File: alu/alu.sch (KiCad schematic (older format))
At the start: 38 parts

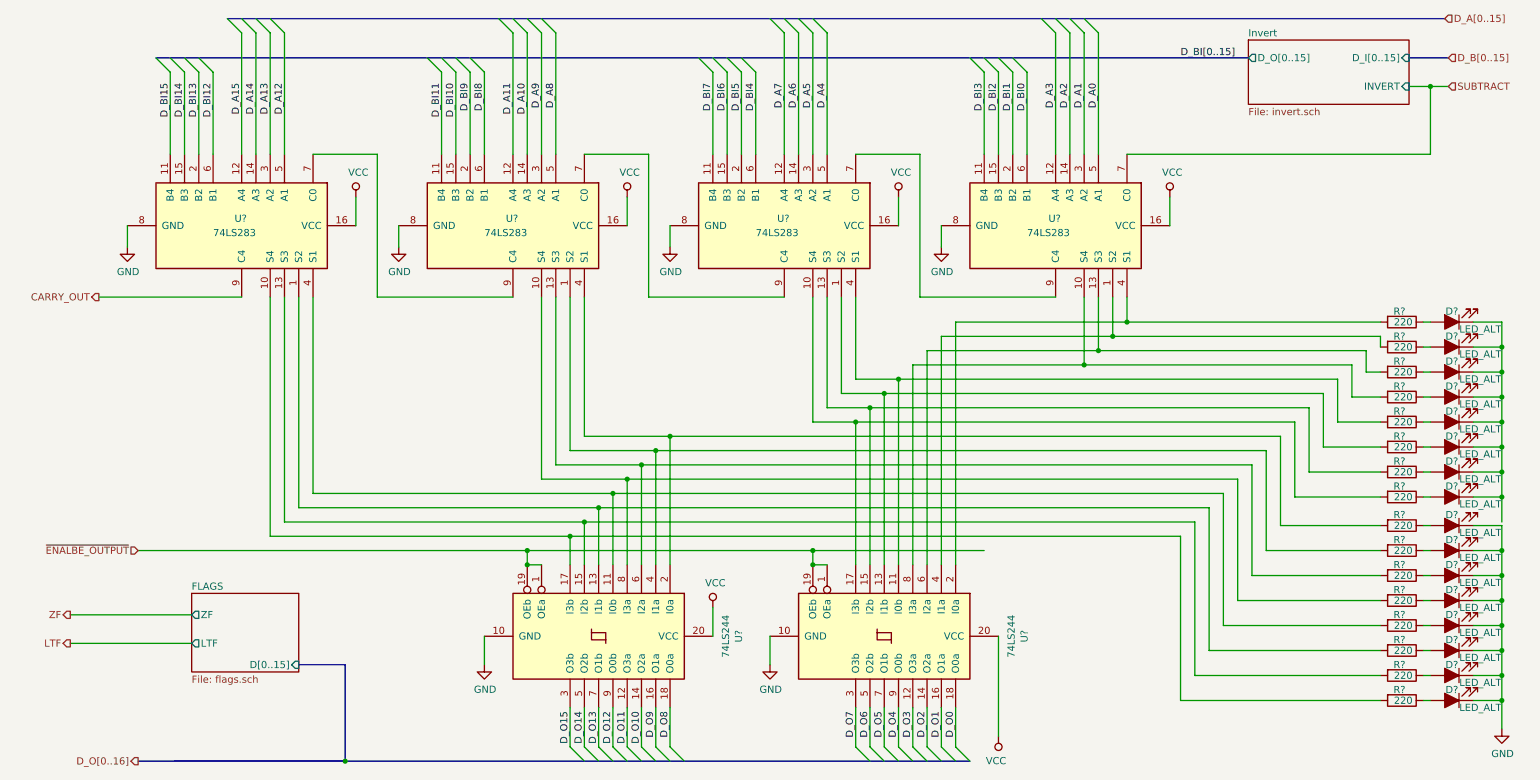
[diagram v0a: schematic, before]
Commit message: alu routed first iteration
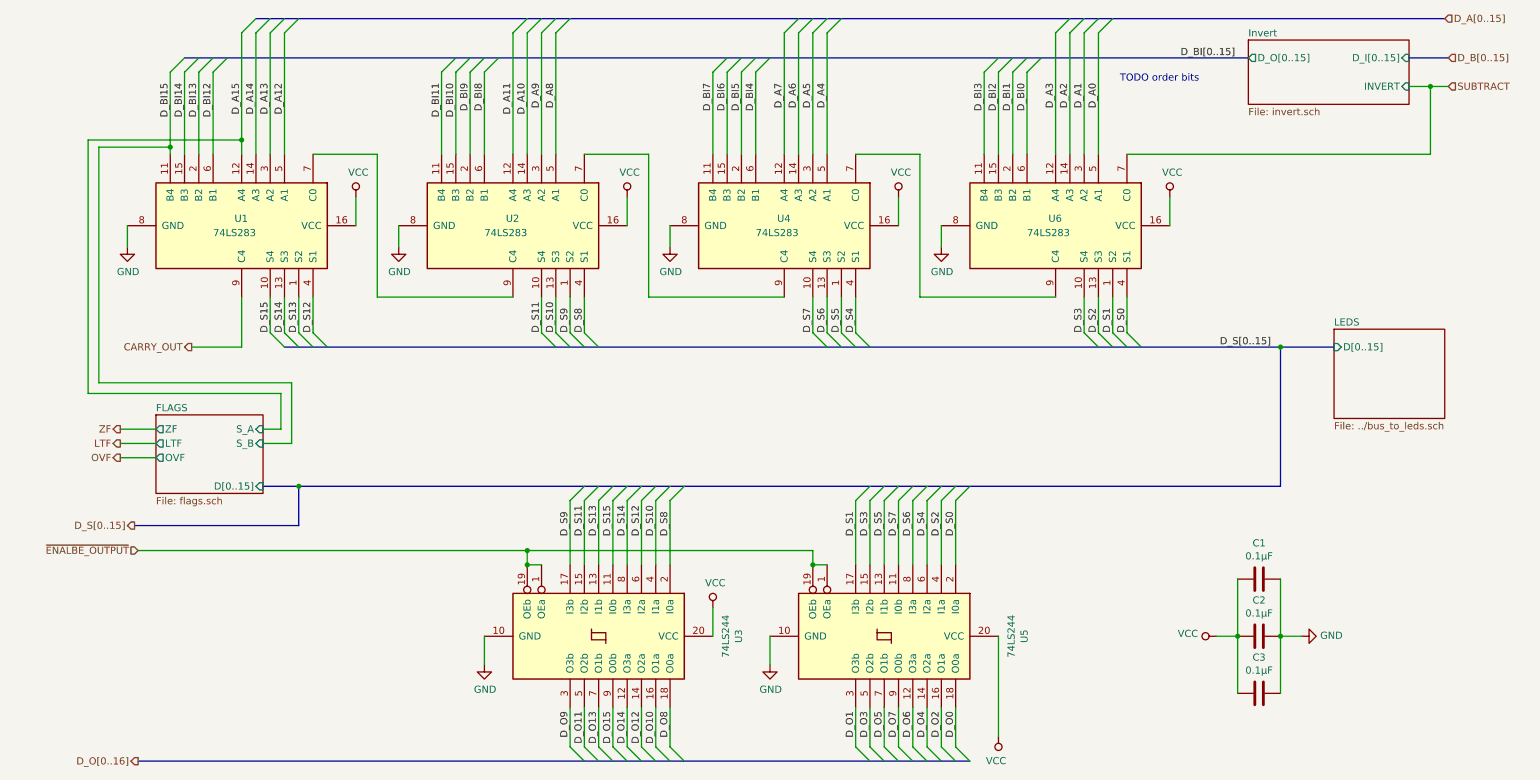
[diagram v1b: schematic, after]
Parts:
- removed D? (x16): LED_ALT, symbol Device:LED_ALT
- removed R? (x16): 220, symbol Device:R
- added C1, C2, C3: 0.1µF, Capacitor_THT:C_Disc_D4.3mm_W1.9mm_P5.00mm, symbol Device:C
- U1, U2, U4, U6: renamed from U?; footprint (none) -> Package_DIP:DIP-16_W7.62mm_LongPads
- U3, U5: renamed from U?; footprint (none) -> Package_DIP:DIP-20_W7.62mm_LongPads
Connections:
- net D_O1: now also U5.3 (O3b); no longer U5.16 (O1a)
- net D_O10: now also U3.16 (O1a); no longer U3.14 (O2a)
- net D_O11: now also U3.5 (O2b); no longer U3.12 (O3a)
- net D_O12: now also U3.14 (O2a); no longer U3.9 (O0b)
- net D_O14: now also U3.12 (O3a); no longer U3.5 (O2b)
- net D_O15: now also U3.9 (O0b); no longer U3.3 (O3b)
- net D_O2: now also U5.16 (O1a); no longer U5.14 (O2a)
- net D_O3: now also U5.5 (O2b); no longer U5.12 (O3a)
- net D_O4: now also U5.14 (O2a); no longer U5.9 (O0b)
- net D_O6: now also U5.12 (O3a); no longer U5.5 (O2b)
- net D_O7: now also U5.9 (O0b); no longer U5.3 (O3b)
- net D_O9: now also U3.3 (O3b); no longer U3.16 (O1a)
- net GND: now also C1.1, C2.1, C3.1
- net VCC: now also C1.2, C2.2, C3.2
- net D_S13: now reaches U1.1 (S2), U3.13 (I1b)
- net D_S15: now reaches U1.10 (S4)
- net D_S15: now also U3.11 (I0b); no longer U3.17 (I3b)
- net D_S11: now reaches U3.15 (I2b)
- net D_S11: now also U2.10 (S4); no longer U1.13 (S3)
- net D_S12: now reaches U1.4 (S1)
- net D_S12: now also U3.6 (I2a); no longer U3.11 (I0b)
- net D_S10: now reaches U3.4 (I1a)
- net D_S10: now also U2.13 (S3); no longer U2.1 (S2)
- net D_S14: now reaches U3.8 (I3a)
- net D_S14: now also U1.13 (S3); no longer U2.10 (S4)
- net D_S8: now reaches U2.4 (S1), U3.2 (I0a)
- net D_S5: now reaches U4.1 (S2), U5.13 (I1b)
- net D_S1: now reaches U5.17 (I3b)
- net D_S1: now also U6.1 (S2); no longer U4.10 (S4)
- net D_S3: now reaches U5.15 (I2b)
- net D_S3: now also U6.10 (S4); no longer U4.13 (S3)
- net D_S4: now reaches U4.4 (S1)
- net D_S4: now also U5.6 (I2a); no longer U5.11 (I0b)
- net D_S2: now reaches U5.4 (I1a)
- net D_S2: now also U6.13 (S3); no longer U6.1 (S2)
- net D_S6: now reaches U5.8 (I3a)
- net D_S6: now also U4.13 (S3); no longer U6.10 (S4)
- net D_S0: now reaches U5.2 (I0a), U6.4 (S1)
- new net D_S7: U4.10 (S4), U5.11 (I0b)
- new net D_S9: U2.1 (S2), U3.17 (I3b)
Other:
- note added: "TODO order bits\n"

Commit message: ram pcb
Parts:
- added C4: 0.1µF, Capacitor_THT:C_Disc_D4.3mm_W1.9mm_P5.00mm, symbol Device:C
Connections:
- net GND: now also C4.1
- net VCC: now also C4.2
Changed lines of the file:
@@
 Text HLabel 1350 4500 0    50   Output ~ 0
 D_S[0..15]
+Text Label 6800 4575 1    50   ~ 0
+D_S6
+$Comp
+L Device:C C4
+U 1 1 5EDF58B1
+P 9225 6075
+F 0 "C4" V 8973 6075 50  0000 C CNN
+F 1 "0.1µF" V 9064 6075 50  0000 C CNN
+F 2 "Capacitor_THT:C_Disc_D4.3mm_W1.9mm_P5.00mm" H 9263 5925 50  0001 C CNN
+F 3 "~" H 9225 6075 50  0001 C CNN
+	1    9225 6075
+	0    1    1    0
+$EndComp
+Wire Wire Line
+	9075 5675 9075 6075
+Connection ~ 9075 5675
+Wire Wire Line
+	9375 6075 9375 5675
+Connection ~ 9375 5675
+Wire Bus Line
+	1700 1225 9150 1225
+Wire Bus Line
+	2200 950  10525 950
 Wire Bus Line
 	2400 3250 9375 3250
@@
 	1375 6150 7200 6150
 Wire Bus Line
-	1700 1225 9150 1225
-Wire Bus Line
-	2200 950  10525 950
-Wire Bus Line
 	2500 4225 9375 4225
-Text Label 6800 4575 1    50   ~ 0
-D_S6
 $EndSCHEMATC

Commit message: Commit uncomitted changes. no clue what I had done last time
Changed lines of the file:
@@
 $Descr A4 11693 8268
 encoding utf-8
-Sheet 6 36
+Sheet 5 36
 Title ""
 Date ""
@@
 AR Path="/5D3352E4/5D35EAC6" Ref="U?"  Part="1"
 AR Path="/5EBD9EFC/5D35EAC6" Ref="U3"  Part="1"
-F 0 "U3" H 4600 6256 50  0000 C CNN
+F 0 "U?" H 4600 6256 50  0000 C CNN
 F 1 "74LS244" H 4600 6165 50  0000 C CNN
 F 2 "Package_DIP:DIP-20_W7.62mm_LongPads" H 4600 5275 50  0001 C CNN
@@
 AR Path="/5D3352E4/5D35F107" Ref="U?"  Part="1"
 AR Path="/5EBD9EFC/5D35F107" Ref="U5"  Part="1"
-F 0 "U5" H 6600 6256 50  0000 C CNN
+F 0 "U?" H 6600 6256 50  0000 C CNN
 F 1 "74LS244" H 6600 6165 50  0000 C CNN
 F 2 "Package_DIP:DIP-20_W7.62mm_LongPads" H 6600 5275 50  0001 C CNN
